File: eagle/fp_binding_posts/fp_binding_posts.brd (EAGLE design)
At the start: 77.6 x 26.6 mm, 6 parts, among them J5 TSM-105-01-S-SV

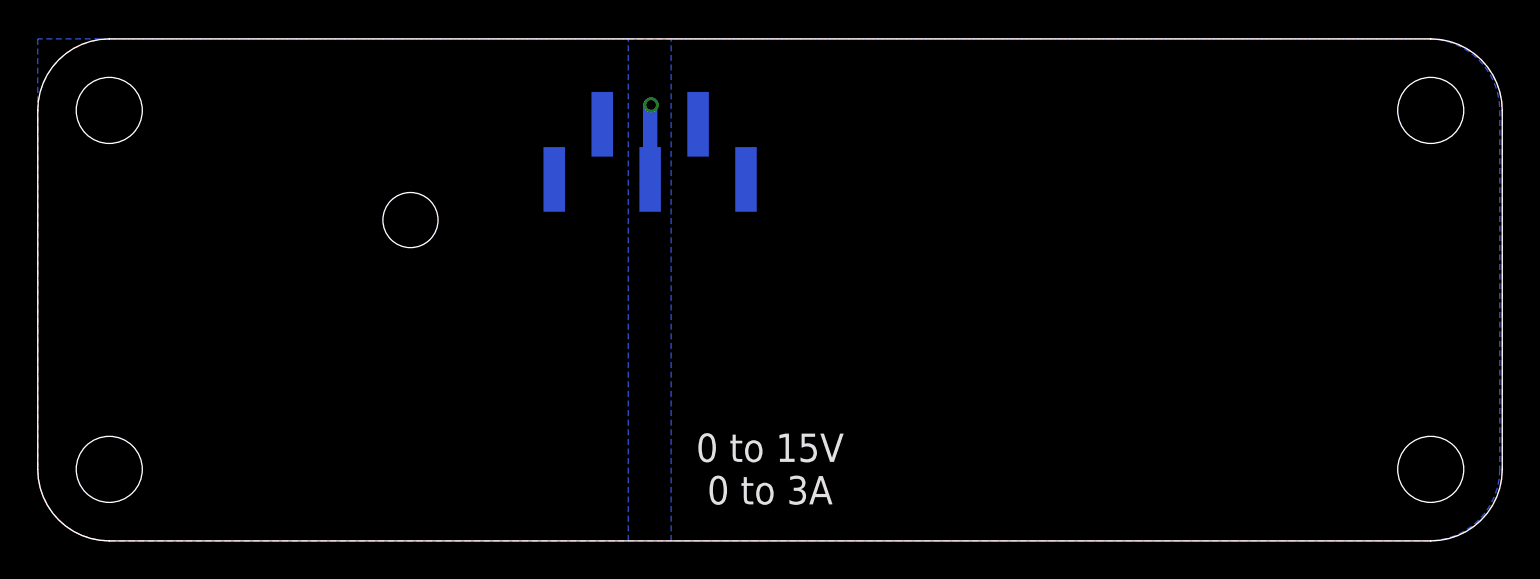
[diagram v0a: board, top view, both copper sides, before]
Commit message: Added binding posts front panel, updated baseline, and published baseline PDF.
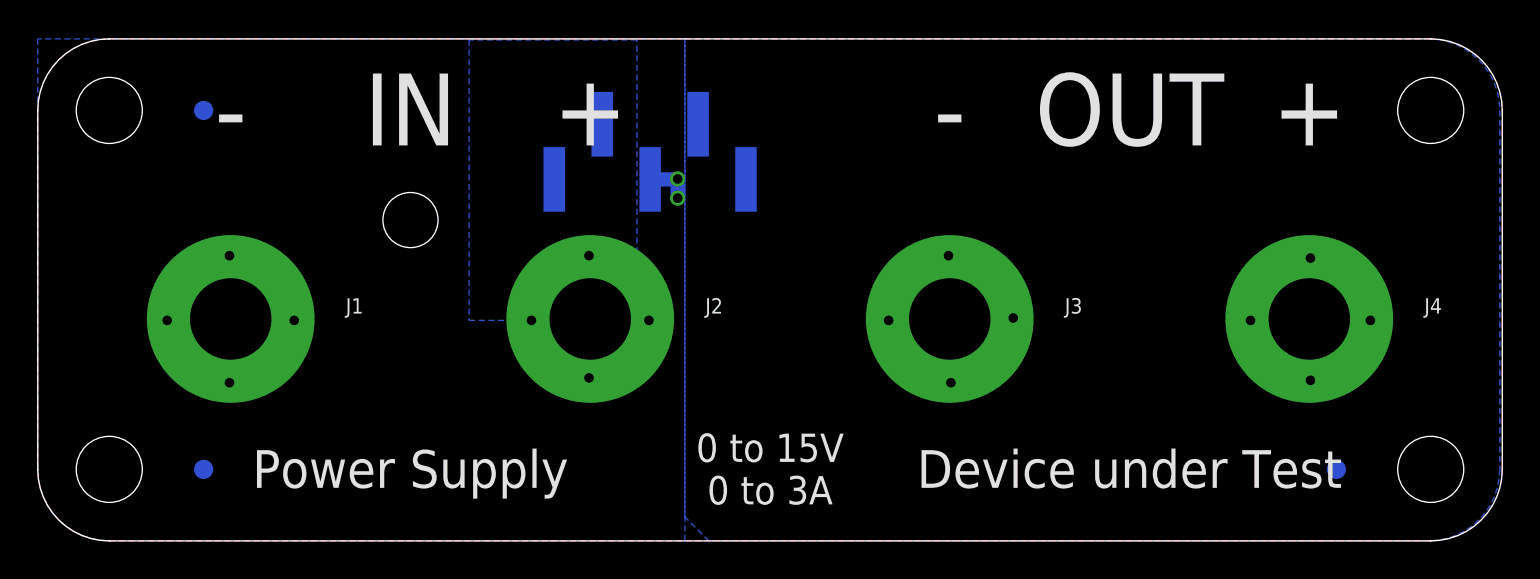
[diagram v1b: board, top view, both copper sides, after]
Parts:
- added FUD1, FUD2, FUD3: FIDUCIAL_1MM, jetperch:FIDUCIAL_1MM_2MM
- added J1, J3: 111-0703-001, jetperch:BINDING_POST_6
- added J2, J4: 111-0702-001, jetperch:BINDING_POST_6
- moved H2 19.0 mm to (3.79, 3.79)
- moved H3 19.0 mm to (3.79, 22.8)
- moved H4 19.0 mm to (73.8, 3.79)
- moved H5 19.0 mm to (73.8, 22.8)
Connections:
- net EXT_IN: now also J2.1
- net EXT_NEG: now also J1.1, J3.1
- net EXT_OUT: now also J4.1
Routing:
- net EXT_NEG: track 3.97 -> 2.48 mm, vias 1 -> 10
- added copper zone on layer 16, net EXT_IN
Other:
- board text added: "+"
- board text added: "-"
- board text added: "Device under Test"
- board text added: "IN"
- board text added: "Joulescope Front Panel: Binding Posts rev A 2019 Jetperch LLC"
- board text added: "OUT"
- board text added: "Power Supply"
- board text removed: "Joulescope Front Panel Reference Baseline Last updated: 2019 Mar 19"
- board text removed: "Joulescope Front Panel: [Type Name] rev [?] 2019 [Your Name]"
